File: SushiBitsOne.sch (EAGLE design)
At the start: 68 parts, among them IC1 STM32F042F6P6, IC2 LM3671-3.3DBV, IC3 TPS562200DBV, J1 ARDUINO_R3, J2 DC-005, Q1 2N7002, Q2 MMBT2222A, U1 STM32F103CBT6-LQFP48, X1 32768Hz, X2 8MHz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

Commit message: Some details of the files are somehow changed?
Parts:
- removed R10, R11, R17: 10k, rcl:R-EU_R0603
- removed R12: 1k, rcl:R-EU_R0603
- removed R16: 4.7k, rcl:R-EU_R0603
- removed R18, R19: 510, rcl:R-EU_R0603
- removed USB1, USB2: ZX62-B-5PA, Seeed-OPL-Connector:MICRO-USB-SMD(ZX62-B-5PA)
- added IC4: (no value), v-reg:XC63FPM
- added J3, J4: (no value), SparkFun-Connectors:USB_MICRO-B_FEMALE-SMT
- added RN2, RN3, RN5: 510, resistor-dil:4R-NEXB38V
- added RN4: 22, resistor-dil:4R-NEXB38V
- C11: value 47u -> 100u; device rcl:CPOL-EUSMCD -> rcl:CPOL-EUUD-8X10
- C14: value 10u -> 22p; device rcl:C-EUC0805 -> rcl:C-EUC0603
- C15: value 47u -> 220u
- C17: value 22p -> 100n
- D1: device diode:DIODE-DO-214AC -> diode:DIODE-DO214AC
- D2, D3: device diode:SCHOTTKY-DIODEDO214AC -> diode:DIODE-SOD123
- J2: value DC-005 -> (none); device Seeed-OPL-Connector:CONN-POWER-JACK-2.1MM(DC-005) -> con-jack:JACK-PLUG0
- LED3, LED4: device led:LEDCHIPLED_0805 -> led:LEDCHIP-LED0805
- R3: value 330 -> 4.7k
- R6: value 4.7k -> 510
- R7: value 22 -> 510
- R8: value 22 -> 10k
- RN1: value 510 -> 22
- Y1: value (none) -> 8M
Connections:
- removed net N$21 (its old number): IC1.PA2, R10.1
- removed net N$26 (its old number): IC1.PB8/BOOT0, R17.2
- removed net TCK: IC1.PA6, RN1B.1
- removed net TDI: IC1.PA7, RN1C.1
- removed net TDO: IC1.PB1, RN1D.1
- removed net TMS: IC1.PA5, RN1A.1
- new net N$23: J3.D-, RN4B.1
- new net N$24: F2.1, J3.VBUS
- new net N$27: C17.1, IC1.AVDD, IC1.VDD, IC4.OUT, RN5B.2, RN5C.2, X4-1.S
- new net N$28: C14.1, IC1.PF0/HSEIN, Y1.1
- new net N$31: IC1.PA6, RN3B.1
- new net N$32: IC1.PA7, RN3C.1
- new net N$33: IC1.PB1, RN3D.1
- new net N$34: IC1.PB8/BOOT0, R8.2
- new net N$37: LED4.A, RN5B.1
- new net N$38: LED3.A, RN5C.1
- net +3V3: now also R5.2, RN2A.1, RN2B.1; no longer IC1.AVDD, IC1.VDD, R18.2, R19.2, X4-1.S
- net D14: now also RN2D.2
- net GND: now also C14.2, IC4.GND, J3.GND, J3.SHIELD, J4.GND, J4.SHIELD, R8.1; no longer R17.1, USB2.SHIELD
- net JTCK: now also RN3B.2; no longer RN1B.2
- net JTDI: now also RN3C.2; no longer RN1C.2
- net JTDO: now also RN3D.2; no longer RN1D.2
- net JTMS: now also RN3A.2; no longer RN1A.2
- net N$1: now also J4.D-
- net N$16: now also IC4.IN
- net N$19: now also RN2D.1
- net N$2: now also J4.D+
- net N$22: now also J3.D+, RN4C.1; no longer IC1.PA3, R11.1
- net N$29: now also C16.1, IC1.PF1/HSEOUT, Y1.2; no longer LED3.A, R18.1
- net N$3: now also RN4B.2; no longer USB2.D-
- net N$30: now also IC1.PA5, RN3A.1; no longer LED4.A, R19.1
- net N$4: now also RN4C.2; no longer USB2.D+
- net N$5: now also IC1.PA2, R6.1; no longer C16.1, IC1.PF0/HSEIN, Y1.1
- net N$6: now also IC1.PA3, R7.1; no longer C17.1, IC1.PF1/HSEOUT, Y1.2
- net N$7: now also RN2A.2
- net N$9: now also RN2B.2
- net RXD: now also R6.2; no longer R10.2
- net TXD: now also R7.2; no longer R11.2
- net VBUS2: now also F1.1, J4.VBUS; no longer F2.1, USB2.VBUS
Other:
- note added: "SushiBits M193v3"
- note removed: "SushiBits M193v4"
- moved on the sheet: C14, C15, C16, C17, LED3, LED4, R3, R5, R6, R7, R8, RN1B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

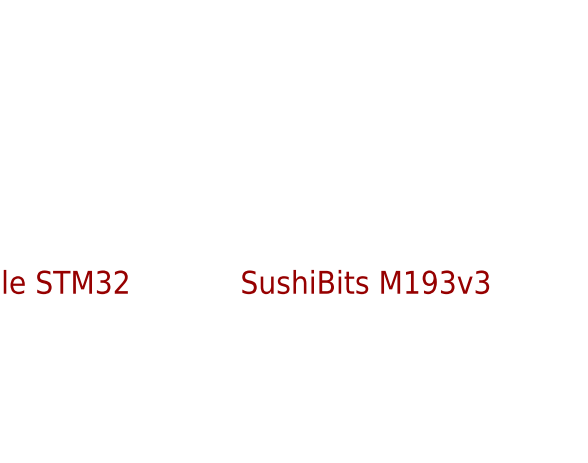
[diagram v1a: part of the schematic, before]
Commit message: I missed the version number on the PDF file
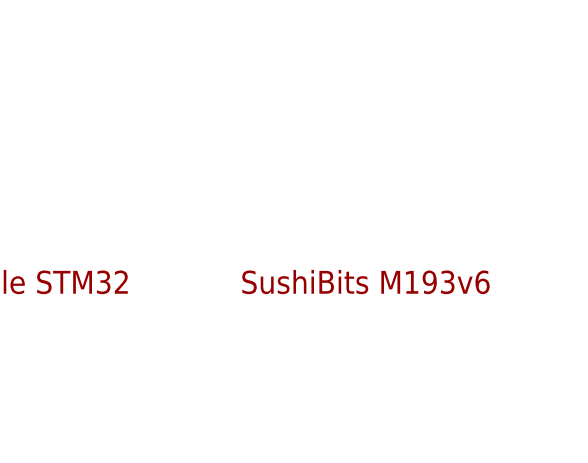
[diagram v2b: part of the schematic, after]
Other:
- note added: "SushiBits M193v6"
- note removed: "SushiBits M193v3"
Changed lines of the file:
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@@
 <text x="162.56" y="22.86" size="2.54" layer="94" align="top-left">Arduino-compatible STM32
 Development Kit</text>
-<text x="217.17" y="22.86" size="2.54" layer="94" align="top-left">SushiBits M193v3</text>
+<text x="217.17" y="22.86" size="2.54" layer="94" align="top-left">SushiBits M193v6</text>
 <text x="5.08" y="5.08" size="2.54" layer="94">Copyright (c) 2016-2017 Max Chan
 Open Source Hardware. Released under 3-caluse BSD license</text>
